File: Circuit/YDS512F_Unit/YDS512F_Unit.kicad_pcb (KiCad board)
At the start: 2 copper layers, 43.5 x 42 mm, 2 parts, among them J1 Conn_01x07_Pin, U1 YDS512F

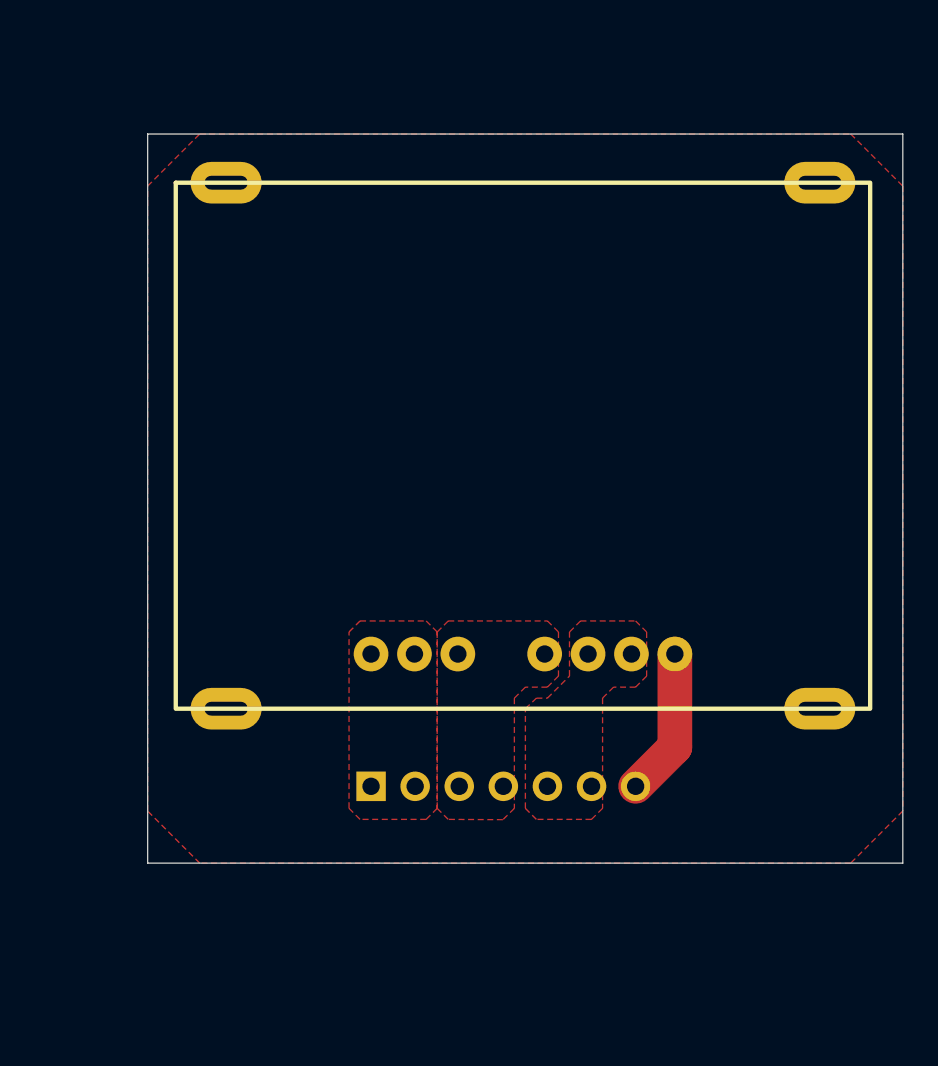
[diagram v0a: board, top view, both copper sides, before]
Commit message: YDS512F基板完成 24V基板とメインモータ基板を微修正
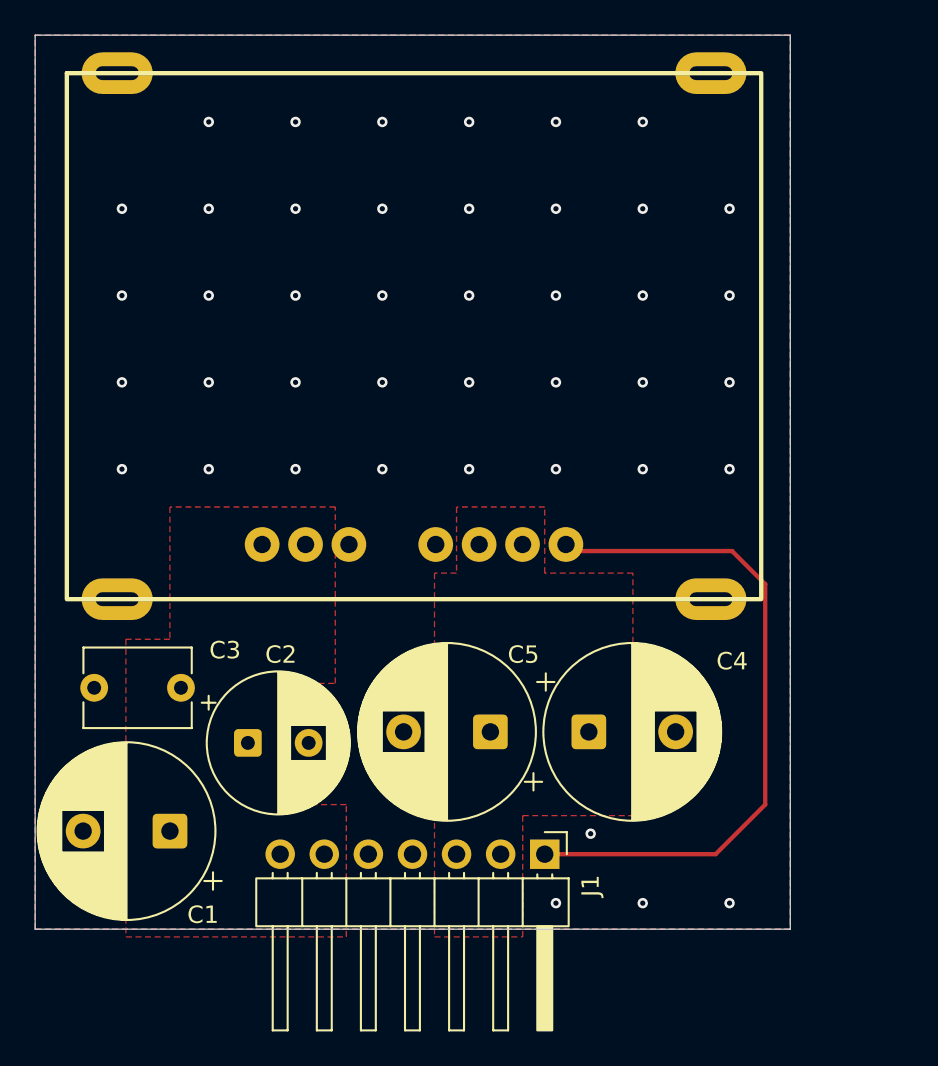
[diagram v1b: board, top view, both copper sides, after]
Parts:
- added C1: 220u, Capacitor_THT:CP_Radial_D10.0mm_P5.00mm, F.Cu at (27.8, 65.8)
- added C2: 47u, Capacitor_THT:CP_Radial_D8.0mm_P3.50mm, F.Cu at (32.3, 60.8)
- added C3: 2.2u, Capacitor_THT:C_Disc_D6.0mm_W4.4mm_P5.00mm, F.Cu at (28.4, 57.6)
- added C4: 100u, Capacitor_THT:CP_Radial_D10.0mm_P5.00mm, F.Cu at (51.9, 60.1)
- added C5: 470u, Capacitor_THT:CP_Radial_D10.0mm_P5.00mm, F.Cu at (46.2, 60.1)
- added G***: LOGO, OU_Picture:OkaLogo, B.Cu at (53.0, 32.0)
- J1: moved to F.Cu
- moved J1 10.7 mm to (49.4, 67.2)
- moved U1 8.90 mm to (41.8, 52.5)
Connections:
- J1 pad 2: Net-(J1-Pin_1) -> Net-(J1-Pin_2)
- J1 pad 3: Net-(J1-Pin_3) -> Net-(J1-Pin_2)
- J1 pad 4: Net-(J1-Pin_3) -> Net-(J1-Pin_4)
- J1 pad 5: Net-(J1-Pin_5) -> Net-(J1-Pin_4)
- J1 pad 6: Net-(J1-Pin_5) -> Net-(J1-Pin_6)
- J1 pad 7: Net-(J1-Pin_7) -> Net-(J1-Pin_6)
- U1 pad 1: Net-(J1-Pin_1) -> Net-(J1-Pin_6)
- U1 pad 2: Net-(J1-Pin_1) -> Net-(J1-Pin_6)
- U1 pad 3: Net-(J1-Pin_3) -> Net-(J1-Pin_4)
- U1 pad 4: Net-(J1-Pin_3) -> Net-(J1-Pin_4)
- U1 pad 5: Net-(J1-Pin_5) -> Net-(J1-Pin_2)
- U1 pad 6: Net-(J1-Pin_5) -> Net-(J1-Pin_2)
- U1 pad 7: Net-(J1-Pin_7) -> Net-(J1-Pin_1)
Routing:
- net Net-(J1-Pin_1): track 0.00 -> 39.0 mm
- net Net-(J1-Pin_7): track 8.56 -> 0.00 mm
- net Net-(J1-Pin_4): vias 0 -> 42
- added copper zone on F.Cu, net Net-(J1-Pin_2)
- added copper zone on B.Cu, net Net-(J1-Pin_4)
- added copper zone on F.Cu, net Net-(J1-Pin_4)
- added copper zone on F.Cu, net Net-(J1-Pin_6)
- removed copper zone on F.Cu, net Net-(J1-Pin_1)
- removed copper zone on F.Cu, net Net-(J1-Pin_3)
- removed copper zone on F.Cu, net Net-(J1-Pin_5)
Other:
- board size 43.5 x 42 mm -> 43.5 x 51.5 mm
- board text added: "2026/06/21"
- board text added: "Board Type:"
- board text added: "Designed by E.Yoshioka ver 1.0"
- board text added: "YDS512F Unit"
- board text removed: "2026/06/17"
- board text removed: "Designed by E.Yoshioka"
- board text removed: "YDS512ユニット"
- board text removed: "岡山大学ロボット研究会"
